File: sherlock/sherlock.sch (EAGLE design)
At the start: 24 parts, among them U3 XBEE-1B2, X1 2540-

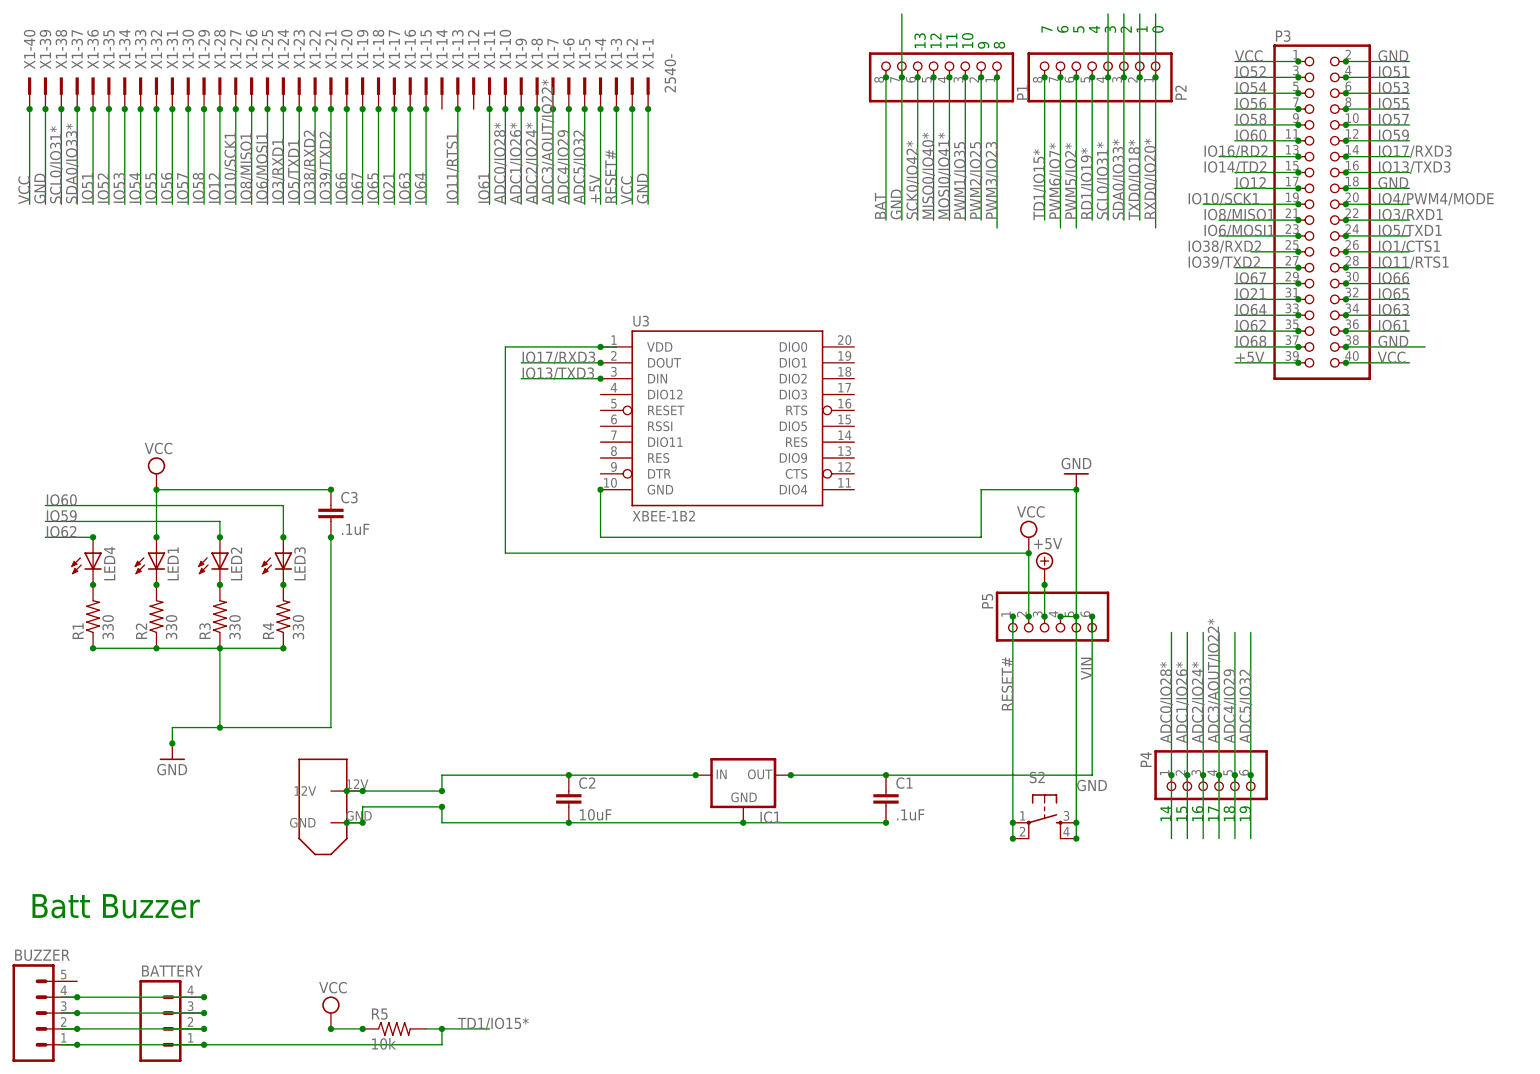
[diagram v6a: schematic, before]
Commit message: Sherlock, Watson, and Solenoid Rev E
- Updated all parts on all boards with their new
  versions in pie.lbr
- Cleaned up silkscreens and made names more
  meaningful
- Cleaned up schematics

This is intended to be the final version for all
three boards. There will be one more revision,
but that is only to add the copyright info Ryan
is making for the schematics and boards.

A side-effect of cleaning up the schematics is
that some connections may have been severd and
traces may have disappeared. I've tried my best
to detect and re-route those traces. If you find
any, please let me know. Thanks.

Sherlock DFM: https://www.freedfm.com/freedfm/0019486703422743/results/summary2.htm
Watson DFM: https://www.freedfm.com/freedfm/0019486703422746/results/summary2.htm
Solenoid DFM: https://www.freedfm.com/freedfm/0019486703422817/results/summary2.htm

Change-Id: I0ddac82c4f4e303a663db72d1e0729480dfd451e
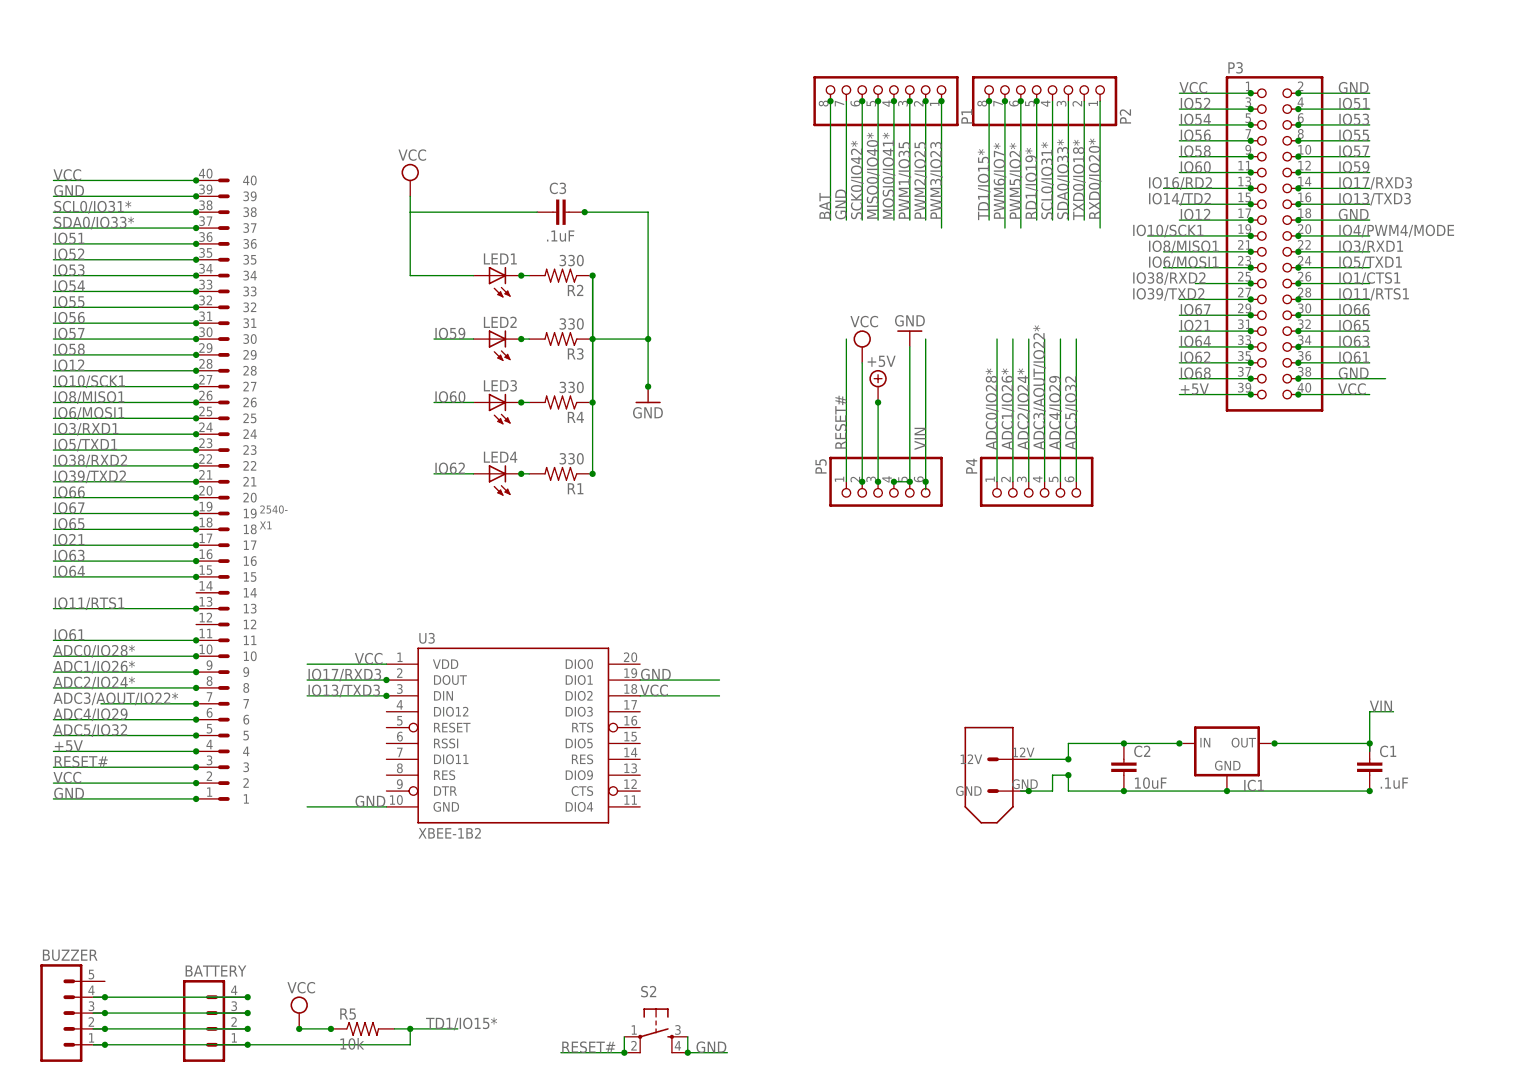
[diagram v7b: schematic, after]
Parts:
- X1: OC_FARNELL unknown -> (none)
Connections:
- net +5V: now also X1.4; no longer X1-4.KL
- net ADC0/IO28*: now also X1.10; no longer X1-10.KL
- net ADC1/IO26*: now also X1.9; no longer X1-9.KL
- net ADC2/IO24*: now also X1.8; no longer X1-8.KL
- net ADC3/AOUT/IO22*: now also X1.7; no longer X1-7.KL
- net ADC4/IO29: now also X1.6; no longer X1-6.KL
- net ADC5/IO32: now also X1.5; no longer X1-5.KL
- net GND: now also U3.DIO1, X1.1, X1.39; no longer X1-1.KL, X1-39.KL
- net IO10/SCK1: now also X1.27; no longer X1-27.KL
- net IO11/RTS1: now also X1.13; no longer X1-13.KL
- net IO12: now also X1.28; no longer X1-28.KL
- net IO21: now also X1.17; no longer X1-17.KL
- net IO3/RXD1: now also X1.24; no longer X1-24.KL
- net IO38/RXD2: now also X1.22; no longer X1-22.KL
- net IO39/TXD2: now also X1.21; no longer X1-21.KL
- net IO5/TXD1: now also X1.23; no longer X1-23.KL
- net IO51: now also X1.36; no longer X1-36.KL
- net IO52: now also X1.35; no longer X1-35.KL
- net IO53: now also X1.34; no longer X1-34.KL
- net IO54: now also X1.33; no longer X1-33.KL
- net IO55: now also X1.32; no longer X1-32.KL
- net IO56: now also X1.31; no longer X1-31.KL
- net IO57: now also X1.30; no longer X1-30.KL
- net IO58: now also X1.29; no longer X1-29.KL
- net IO6/MOSI1: now also X1.25; no longer X1-25.KL
- net IO61: now also X1.11; no longer X1-11.KL
- net IO63: now also X1.16; no longer X1-16.KL
- net IO64: now also X1.15; no longer X1-15.KL
- net IO65: now also X1.18; no longer X1-18.KL
- net IO66: now also X1.20; no longer X1-20.KL
- net IO67: now also X1.19; no longer X1-19.KL
- net IO8/MISO1: now also X1.26; no longer X1-26.KL
- net RESET#: now also X1.3; no longer X1-3.KL
- net SCL0/IO31*: now also X1.38; no longer X1-38.KL
- net SDA0/IO33*: now also X1.37; no longer X1-37.KL
- net VCC: now also U3.DIO2, X1.2, X1.40; no longer X1-2.KL, X1-40.KL
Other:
- note added: "Battery Buzzer"
- note added: "Power"
- note added: "Regulator"
- note added: "Reset"
- note added: "Voltage"
- note added: "Watson"
- note removed: "0"
- note removed: "1"
- note removed: "10"
- note removed: "11"
- note removed: "12"
- note removed: "13"
- note removed: "14"
- note removed: "15"
- note removed: "16"
- note removed: "17"
- note removed: "18"
- note removed: "19"
- note removed: "2"
- note removed: "3"
- note removed: "4"
- note removed: "5"
- note removed: "6"
- note removed: "7"
- note removed: "8"
- note removed: "9"
- note removed: "Batt Buzzer"
- moved on the sheet: BATTERY, BUZZER, C1, C2, C3, IC1, LED1, LED2, LED3, LED4, P1, P2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

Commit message: Sherlock/Watson/Solenoid Rev E (Again)
Had to make a few simple changes Dennis requested.
This is the final version. Rev F will only contain
extra copyright material.

Sherlcok DFM: https://www.freedfm.com/freedfm/0019486703424644/results/summary2.htm
Watson DFM: https://www.freedfm.com/freedfm/0019486703424641/results/summary2.htm
Solenoid DFM: https://www.freedfm.com/freedfm/0019486703424640/results/summary2.htm

Change-Id: Ibaa3e17f4a8e9033ce9bcff25cf747d321aea476
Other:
- note added: "To Watson"
- note removed: "Watson"
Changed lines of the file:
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@@
 <setting verticaltext="up"/>
 </settings>
-<grid distance="0.05" unitdist="inch" unit="inch" style="lines" multiple="1" display="no" altdistance="0.01" altunitdist="inch" altunit="inch"/>
+<grid distance="0.1" unitdist="inch" unit="inch" style="lines" multiple="1" display="no" altdistance="0.01" altunitdist="inch" altunit="inch"/>
 <layers>
 <layer number="1" name="Top" color="4" fill="1" visible="no" active="no"/>
@@
 <text x="134.62" y="55.88" size="6.4516" layer="100">Power</text>
 <text x="185.42" y="68.58" size="6.4516" layer="100">Regulator</text>
-<text x="15.24" y="161.29" size="6.4516" layer="100">Watson</text>
+<text x="10.16" y="161.29" size="6.4516" layer="100">To Watson</text>
 <text x="13.97" y="34.29" size="6.4516" layer="100">Battery Buzzer</text>
 <text x="189.23" y="77.47" size="6.4516" layer="100">Voltage</text>
